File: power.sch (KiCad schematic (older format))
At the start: 8 parts, among them U24 TLV62569P

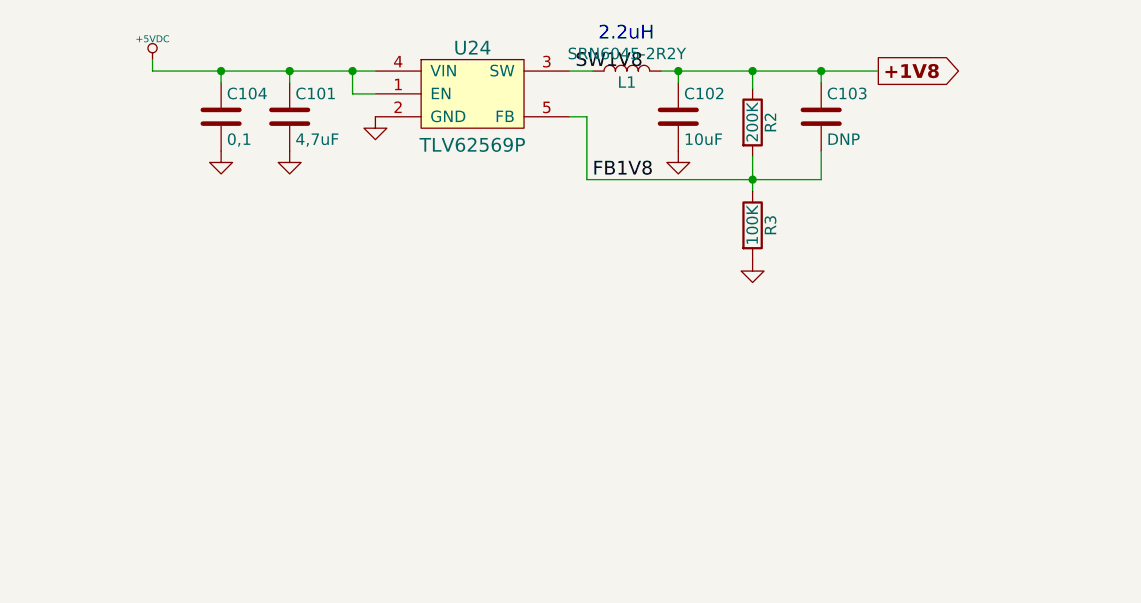
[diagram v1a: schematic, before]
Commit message: +3V3 PSU
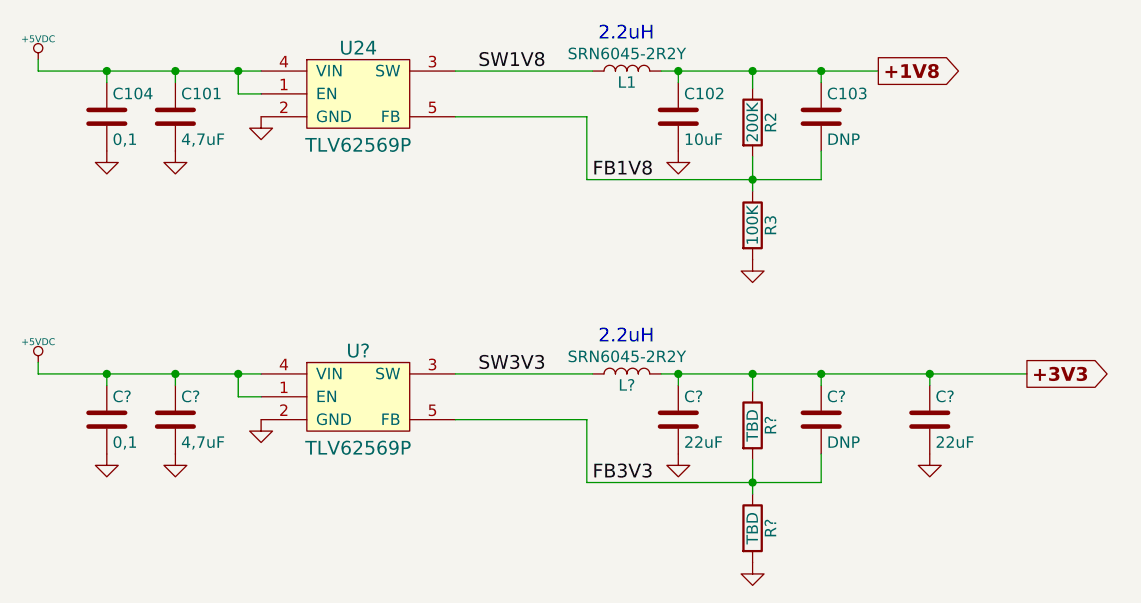
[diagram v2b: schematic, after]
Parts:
- added C?: 4,7uF, Capacitors_SMD:C_0805, symbol C
- added C? (x2): 22uF, Capacitors_Tantalum_SMD:CP_Tantalum_Case-B_EIA-3528-21_Reflow, symbol C
- added C?: DNP, Capacitors_SMD:C_0603, symbol C
- added C?: 0,1, Capacitors_SMD:C_0603, symbol C
- added L?: SRN6045-2R2Y, zorro:SRN6045, symbol L
- added R? (x2): TBD, Resistors_SMD:R_0603, symbol R
- added U?: TLV62569P, TO_SOT_Packages_SMD:SOT-23-5, symbol TLV62569P
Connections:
- net +5VDC: now also C?.1, C?.1, U?.1 (EN), U?.4 (VIN)
- net GND: now also C?.2, C?.2, C?.2, C?.2, R?.2, U?.2 (GND)
- new net +3V3: C?.1, C?.1, C?.1, L?.2, R?.1
- new net FB3V3: C?.2, R?.1, R?.2, U?.5 (FB)
- new net SW3V3: L?.1, U?.3 (SW)
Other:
- moved on the sheet: C101, C104, U24

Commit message: +3V3 placement and early routing
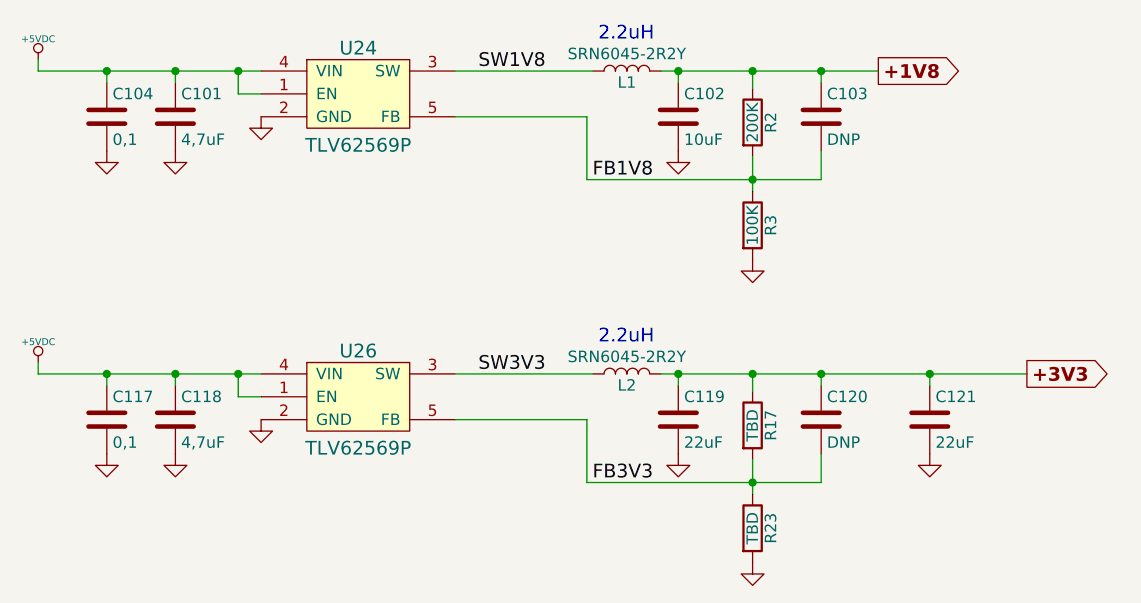
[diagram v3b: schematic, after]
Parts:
- gave numbers to parts that had none: 9
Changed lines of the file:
@@
 $EndComp
 $Comp
-L GND #PWR0178
+L GND #PWR179
 U 1 1 588CA667
 P 4500 3850
-F 0 "#PWR0178" H 4500 3600 50  0001 C CNN
+F 0 "#PWR179" H 4500 3600 50  0001 C CNN
 F 1 "GND" H 4500 3700 50  0001 C CNN
 F 2 "" H 4500 3850 50  0000 C CNN
@@
 	4500 3750 4400 3750
 Wire Wire Line
-	4400 3650 4400 3750
+	4400 3750 4400 3650
 Wire Wire Line
 	3525 3650 4500 3650
@@
 Connection ~ 4125 3650
 $Comp
-L GND #PWR0179
+L GND #PWR181
 U 1 1 588CA72B
 P 4125 4000
-F 0 "#PWR0179" H 4125 3750 50  0001 C CNN
+F 0 "#PWR181" H 4125 3750 50  0001 C CNN
 F 1 "GND" H 4125 3850 50  0001 C CNN
 F 2 "" H 4125 4000 50  0000 C CNN
@@
 	6650 4025 6650 4175
 $Comp
-L GND #PWR0180
+L GND #PWR183
 U 1 1 588CB06D
 P 6650 4475
-F 0 "#PWR0180" H 6650 4225 50  0001 C CNN
+F 0 "#PWR183" H 6650 4225 50  0001 C CNN
 F 1 "GND" H 6650 4325 50  0001 C CNN
 F 2 "" H 6650 4475 50  0000 C CNN
@@
 $EndComp
 $Comp
-L GND #PWR0181
+L GND #PWR182
 U 1 1 588CB1AB
 P 6325 4000
-F 0 "#PWR0181" H 6325 3750 50  0001 C CNN
+F 0 "#PWR182" H 6325 3750 50  0001 C CNN
 F 1 "GND" H 6325 3850 50  0001 C CNN
 F 2 "" H 6325 4000 50  0000 C CNN
@@
 +1V8
 $Comp
-L +5VDC #PWR0182
+L +5VDC #PWR178
 U 1 1 588CF502
 P 3525 3600
-F 0 "#PWR0182" H 3625 3650 20  0001 C CNN
+F 0 "#PWR178" H 3625 3650 20  0001 C CNN
 F 1 "+5VDC" H 3525 3690 30  0000 C CNN
 F 2 "" H 3525 3600 60  0000 C CNN
@@
 Connection ~ 3825 3650
 $Comp
-L GND #PWR0183
+L GND #PWR180
 U 1 1 588D28B5
 P 3825 4000
-F 0 "#PWR0183" H 3825 3750 50  0001 C CNN
+F 0 "#PWR180" H 3825 3750 50  0001 C CNN
 F 1 "GND" H 3825 3850 50  0001 C CNN
 F 2 "" H 3825 4000 50  0000 C CNN
@@
 SW1V8
 $Comp
-L TLV62569P U?
+L TLV62569P U26
 U 1 1 58A65160
 P 4925 5075
-F 0 "U?" H 4925 5275 60  0000 C CNN
+F 0 "U26" H 4925 5275 60  0000 C CNN
 F 1 "TLV62569P" H 4925 4850 60  0000 C CNN
 F 2 "TO_SOT_Packages_SMD:SOT-23-5" H 4925 5075 60  0001 C CNN
@@
 $EndComp
 $Comp
-L GND #PWR?
+L GND #PWR185
 U 1 1 58A65167
 P 4500 5175
-F 0 "#PWR?" H 4500 4925 50  0001 C CNN
+F 0 "#PWR185" H 4500 4925 50  0001 C CNN
 F 1 "GND" H 4500 5025 50  0001 C CNN
 F 2 "" H 4500 5175 50  0000 C CNN
@@
 	4500 5075 4400 5075
 Wire Wire Line
-	4400 4975 4400 5075
+	4400 5075 4400 4975
 Wire Wire Line
 	3525 4975 4500 4975
 Connection ~ 4400 4975
 $Comp
-L C C?
+L C C118
 U 1 1 58A65174
 P 4125 5175
-F 0 "C?" H 4150 5275 50  0000 L CNN
+F 0 "C118" H 4150 5275 50  0000 L CNN
 F 1 "4,7uF" H 4150 5075 50  0000 L CNN
 F 2 "Capacitors_SMD:C_0805" H 4163 5025 50  0001 C CNN
@@
 Connection ~ 4125 4975
 $Comp
-L GND #PWR?
+L GND #PWR187
 U 1 1 58A6517D
 P 4125 5325
-F 0 "#PWR?" H 4125 5075 50  0001 C CNN
+F 0 "#PWR187" H 4125 5075 50  0001 C CNN
 F 1 "GND" H 4125 5175 50  0001 C CNN
 F 2 "" H 4125 5325 50  0000 C CNN
@@
 $EndComp
 $Comp
-L L L?
+L L L2
 U 1 1 58A65183
 P 6100 4975
-F 0 "L?" V 6050 4975 50  0000 C CNN
+F 0 "L2" V 6050 4975 50  0000 C CNN
 F 1 "SRN6045-2R2Y" V 6175 4975 50  0000 C CNN
 F 2 "zorro:SRN6045" H 6100 4975 50  0001 C CNN
@@
 	6250 4975 7850 4975
 $Comp
-L R R?
+L R R17
 U 1 1 58A6518E
 P 6650 5200
-F 0 "R?" V 6730 5200 50  0000 C CNN
+F 0 "R17" V 6730 5200 50  0000 C CNN
 F 1 "TBD" V 6650 5200 50  0000 C CNN
 F 2 "Resistors_SMD:R_0603" V 6580 5200 50  0001 C CNN
@@
 Connection ~ 6650 4975
 $Comp
-L R R?
+L R R23
 U 1 1 58A65196
 P 6650 5650
-F 0 "R?" V 6730 5650 50  0000 C CNN
+F 0 "R23" V 6730 5650 50  0000 C CNN
 F 1 "TBD" V 6650 5650 50  0000 C CNN
 F 2 "Resistors_SMD:R_0603" V 6580 5650 50  0001 C CNN
@@
 	6650 5350 6650 5500
 $Comp
-L GND #PWR?
+L GND #PWR190
 U 1 1 58A6519F
 P 6650 5800
-F 0 "#PWR?" H 6650 5550 50  0001 C CNN
+F 0 "#PWR190" H 6650 5550 50  0001 C CNN
 F 1 "GND" H 6650 5650 50  0001 C CNN
 F 2 "" H 6650 5800 50  0000 C CNN
@@
 Connection ~ 6650 5450
 $Comp
-L C C?
+L C C119
 U 1 1 58A651AA
 P 6325 5175
-F 0 "C?" H 6350 5275 50  0000 L CNN
+F 0 "C119" H 6350 5275 50  0000 L CNN
 F 1 "22uF" H 6350 5075 50  0000 L CNN
 F 2 "Capacitors_Tantalum_SMD:CP_Tantalum_Case-B_EIA-3528-21_Reflow" H 6363 5025 50  0001 C CNN
@@
 $EndComp
 $Comp
-L GND #PWR?
+L GND #PWR188
 U 1 1 58A651B1
 P 6325 5325
-F 0 "#PWR?" H 6325 5075 50  0001 C CNN
+F 0 "#PWR188" H 6325 5075 50  0001 C CNN
 F 1 "GND" H 6325 5175 50  0001 C CNN
 F 2 "" H 6325 5325 50  0000 C CNN
@@
 Connection ~ 6325 4975
 $Comp
-L C C?
+L C C120
 U 1 1 58A651B9
 P 6950 5175
-F 0 "C?" H 6975 5275 50  0000 L CNN
+F 0 "C120" H 6975 5275 50  0000 L CNN
 F 1 "DNP" H 6975 5075 50  0000 L CNN
 F 2 "Capacitors_SMD:C_0603" H 6988 5025 50  0001 C CNN
@@
 +3V3
 $Comp
-L +5VDC #PWR?
+L +5VDC #PWR184
 U 1 1 58A651C3
 P 3525 4925
-F 0 "#PWR?" H 3625 4975 20  0001 C CNN
+F 0 "#PWR184" H 3625 4975 20  0001 C CNN
 F 1 "+5VDC" H 3525 5015 30  0000 C CNN
 F 2 "" H 3525 4925 60  0000 C CNN
@@
 	3525 4925 3525 4975
 $Comp
-L C C?
+L C C117
 U 1 1 58A651CA
 P 3825 5175
-F 0 "C?" H 3850 5275 50  0000 L CNN
+F 0 "C117" H 3850 5275 50  0000 L CNN
 F 1 "0,1" H 3850 5075 50  0000 L CNN
 F 2 "Capacitors_SMD:C_0603" H 3863 5025 50  0001 C CNN
@@
 Connection ~ 3825 4975
 $Comp
-L GND #PWR?
+L GND #PWR186
 U 1 1 58A651D3
 P 3825 5325
-F 0 "#PWR?" H 3825 5075 50  0001 C CNN
+F 0 "#PWR186" H 3825 5075 50  0001 C CNN
 F 1 "GND" H 3825 5175 50  0001 C CNN
 F 2 "" H 3825 5325 50  0000 C CNN
@@
 SW3V3
 $Comp
-L C C?
+L C C121
 U 1 1 58A65DDC
 P 7425 5175
-F 0 "C?" H 7450 5275 50  0000 L CNN
+F 0 "C121" H 7450 5275 50  0000 L CNN
 F 1 "22uF" H 7450 5075 50  0000 L CNN
 F 2 "Capacitors_Tantalum_SMD:CP_Tantalum_Case-B_EIA-3528-21_Reflow" H 7463 5025 50  0001 C CNN
@@
 $EndComp
 $Comp
-L GND #PWR?
+L GND #PWR189
 U 1 1 58A65EC4
 P 7425 5325
-F 0 "#PWR?" H 7425 5075 50  0001 C CNN
+F 0 "#PWR189" H 7425 5075 50  0001 C CNN
 F 1 "GND" H 7425 5175 50  0001 C CNN
 F 2 "" H 7425 5325 50  0000 C CNN

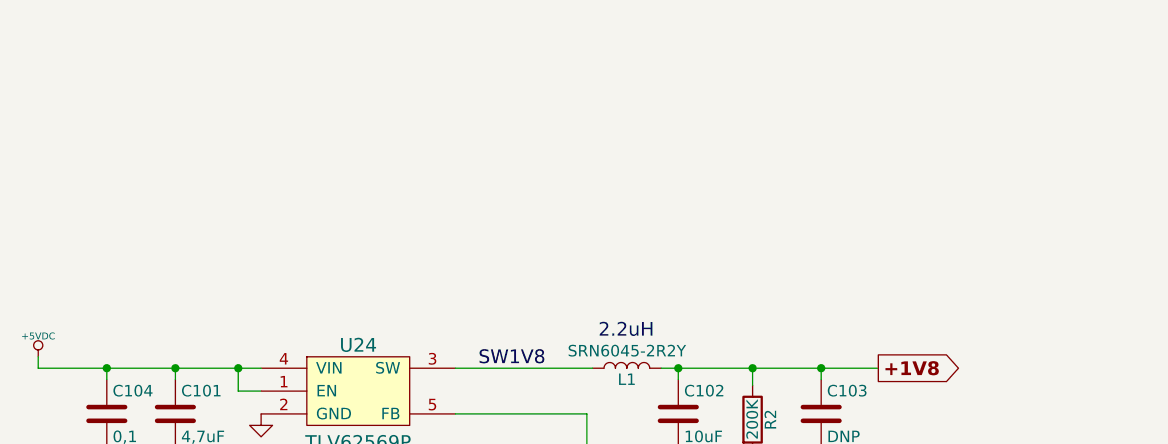
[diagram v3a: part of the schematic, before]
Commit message: Added VCCINT power supply
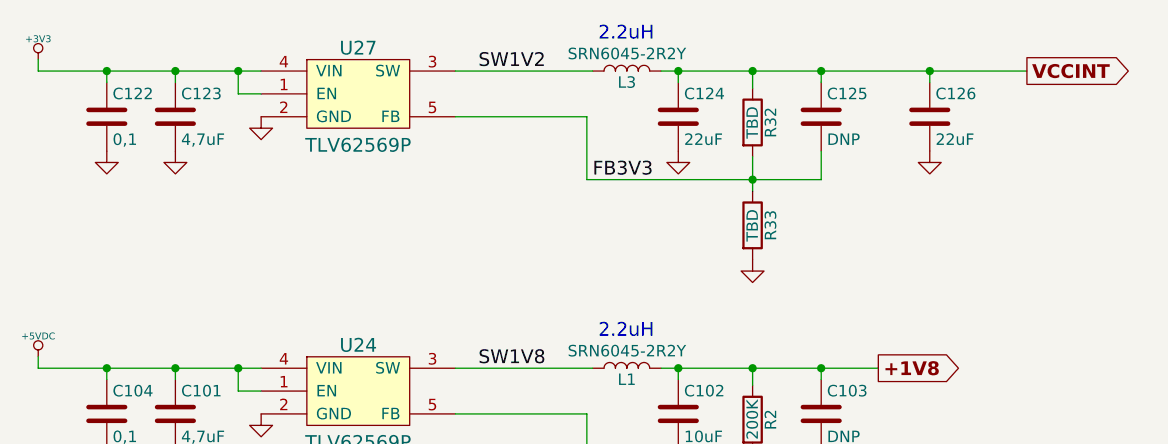
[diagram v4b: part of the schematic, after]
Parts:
- added C122: 0,1, Capacitors_SMD:C_0603, symbol C
- added C123: 4,7uF, Capacitors_SMD:C_0805, symbol C
- added C124, C126: 22uF, Capacitors_Tantalum_SMD:CP_Tantalum_Case-B_EIA-3528-21_Reflow, symbol C
- added C125: DNP, Capacitors_SMD:C_0603, symbol C
- added L3: SRN6045-2R2Y, zorro:SRN6045, symbol L
- added R32, R33: TBD, Resistors_SMD:R_0603, symbol R
- added U27: TLV62569P, TO_SOT_Packages_SMD:SOT-23-5, symbol TLV62569P
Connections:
- net +3V3: now also C122.1, C123.1, U27.1 (EN), U27.4 (VIN)
- net FB3V3: now also C125.2, R32.2, R33.1, U27.5 (FB)
- net GND: now also C122.2, C123.2, C124.2, C126.2, R33.2, U27.2 (GND)
- new net SW1V2: L3.1, U27.3 (SW)
- new net VCCINT: C124.1, C125.1, C126.1, L3.2, R32.1

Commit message: Up
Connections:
- net FB3V3: no longer C125.2, R32.2, R33.1, U27.5 (FB)
- new net FB1V2: C125.2, R32.2, R33.1, U27.5 (FB)
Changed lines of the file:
@@
 $EndComp
 $Comp
-L GND #PWR188
+L GND #PWR0181
 U 1 1 588CA667
 P 4500 3850
-F 0 "#PWR188" H 4500 3600 50  0001 C CNN
+F 0 "#PWR0181" H 4500 3600 50  0001 C CNN
 F 1 "GND" H 4500 3700 50  0001 C CNN
 F 2 "" H 4500 3850 50  0000 C CNN
@@
 Connection ~ 4125 3650
 $Comp
-L GND #PWR185
+L GND #PWR0182
 U 1 1 588CA72B
 P 4125 4000
-F 0 "#PWR185" H 4125 3750 50  0001 C CNN
+F 0 "#PWR0182" H 4125 3750 50  0001 C CNN
 F 1 "GND" H 4125 3850 50  0001 C CNN
 F 2 "" H 4125 4000 50  0000 C CNN
@@
 	6650 4025 6650 4175
 $Comp
-L GND #PWR194
+L GND #PWR0183
 U 1 1 588CB06D
 P 6650 4475
-F 0 "#PWR194" H 6650 4225 50  0001 C CNN
+F 0 "#PWR0183" H 6650 4225 50  0001 C CNN
 F 1 "GND" H 6650 4325 50  0001 C CNN
 F 2 "" H 6650 4475 50  0000 C CNN
@@
 $EndComp
 $Comp
-L GND #PWR191
+L GND #PWR0184
 U 1 1 588CB1AB
 P 6325 4000
-F 0 "#PWR191" H 6325 3750 50  0001 C CNN
+F 0 "#PWR0184" H 6325 3750 50  0001 C CNN
 F 1 "GND" H 6325 3850 50  0001 C CNN
 F 2 "" H 6325 4000 50  0000 C CNN
@@
 +1V8
 $Comp
-L +5VDC #PWR179
+L +5VDC #PWR0185
 U 1 1 588CF502
 P 3525 3600
-F 0 "#PWR179" H 3625 3650 20  0001 C CNN
+F 0 "#PWR0185" H 3625 3650 20  0001 C CNN
 F 1 "+5VDC" H 3525 3690 30  0000 C CNN
 F 2 "" H 3525 3600 60  0000 C CNN
@@
 Connection ~ 3825 3650
 $Comp
-L GND #PWR182
+L GND #PWR0186
 U 1 1 588D28B5
 P 3825 4000
-F 0 "#PWR182" H 3825 3750 50  0001 C CNN
+F 0 "#PWR0186" H 3825 3750 50  0001 C CNN
 F 1 "GND" H 3825 3850 50  0001 C CNN
 F 2 "" H 3825 4000 50  0000 C CNN
@@
 $EndComp
 $Comp
-L GND #PWR189
+L GND #PWR0187
 U 1 1 58A65167
 P 4500 5175
-F 0 "#PWR189" H 4500 4925 50  0001 C CNN
+F 0 "#PWR0187" H 4500 4925 50  0001 C CNN
 F 1 "GND" H 4500 5025 50  0001 C CNN
 F 2 "" H 4500 5175 50  0000 C CNN
@@
 Connection ~ 4125 4975
 $Comp
-L GND #PWR186
+L GND #PWR0188
 U 1 1 58A6517D
 P 4125 5325
-F 0 "#PWR186" H 4125 5075 50  0001 C CNN
+F 0 "#PWR0188" H 4125 5075 50  0001 C CNN
 F 1 "GND" H 4125 5175 50  0001 C CNN
 F 2 "" H 4125 5325 50  0000 C CNN
@@
 	6650 5350 6650 5500
 $Comp
-L GND #PWR195
+L GND #PWR0189
 U 1 1 58A6519F
 P 6650 5800
-F 0 "#PWR195" H 6650 5550 50  0001 C CNN
+F 0 "#PWR0189" H 6650 5550 50  0001 C CNN
 F 1 "GND" H 6650 5650 50  0001 C CNN
 F 2 "" H 6650 5800 50  0000 C CNN
@@
 $EndComp
 $Comp
-L GND #PWR192
+L GND #PWR0190
 U 1 1 58A651B1
 P 6325 5325
-F 0 "#PWR192" H 6325 5075 50  0001 C CNN
+F 0 "#PWR0190" H 6325 5075 50  0001 C CNN
 F 1 "GND" H 6325 5175 50  0001 C CNN
 F 2 "" H 6325 5325 50  0000 C CNN
@@
 Connection ~ 3825 4975
 $Comp
-L GND #PWR183
+L GND #PWR0191
 U 1 1 58A651D3
 P 3825 5325
-F 0 "#PWR183" H 3825 5075 50  0001 C CNN
+F 0 "#PWR0191" H 3825 5075 50  0001 C CNN
 F 1 "GND" H 3825 5175 50  0001 C CNN
 F 2 "" H 3825 5325 50  0000 C CNN
@@
 $EndComp
 $Comp
-L GND #PWR197
+L GND #PWR0192
 U 1 1 58A65EC4
 P 7425 5325
-F 0 "#PWR197" H 7425 5075 50  0001 C CNN
+F 0 "#PWR0192" H 7425 5075 50  0001 C CNN
 F 1 "GND" H 7425 5175 50  0001 C CNN
 F 2 "" H 7425 5325 50  0000 C CNN
@@
 Connection ~ 7425 4975
 $Comp
-L +5VDC #PWR180
+L +5VDC #PWR0193
 U 1 1 58A651C3
 P 3525 4925
-F 0 "#PWR180" H 3625 4975 20  0001 C CNN
+F 0 "#PWR0193" H 3625 4975 20  0001 C CNN
 F 1 "+5VDC" H 3525 5015 30  0000 C CNN
 F 2 "" H 3525 4925 60  0000 C CNN
@@
 $EndComp
 $Comp
-L GND #PWR187
+L GND #PWR0194
 U 1 1 58A865FA
 P 4500 2550
-F 0 "#PWR187" H 4500 2300 50  0001 C CNN
+F 0 "#PWR0194" H 4500 2300 50  0001 C CNN
 F 1 "GND" H 4500 2400 50  0001 C CNN
 F 2 "" H 4500 2550 50  0000 C CNN
@@
 Connection ~ 4125 2350
 $Comp
-L GND #PWR184
+L GND #PWR0195
 U 1 1 58A8660D
 P 4125 2700
-F 0 "#PWR184" H 4125 2450 50  0001 C CNN
+F 0 "#PWR0195" H 4125 2450 50  0001 C CNN
 F 1 "GND" H 4125 2550 50  0001 C CNN
 F 2 "" H 4125 2700 50  0000 C CNN
@@
 	6650 2725 6650 2875
 $Comp
-L GND #PWR193
+L GND #PWR0196
 U 1 1 58A8662B
 P 6650 3175
-F 0 "#PWR193" H 6650 2925 50  0001 C CNN
+F 0 "#PWR0196" H 6650 2925 50  0001 C CNN
 F 1 "GND" H 6650 3025 50  0001 C CNN
 F 2 "" H 6650 3175 50  0000 C CNN
@@
 $EndComp
 $Comp
-L GND #PWR190
+L GND #PWR0197
 U 1 1 58A8663C
 P 6325 2700
-F 0 "#PWR190" H 6325 2450 50  0001 C CNN
+F 0 "#PWR0197" H 6325 2450 50  0001 C CNN
 F 1 "GND" H 6325 2550 50  0001 C CNN
 F 2 "" H 6325 2700 50  0000 C CNN
@@
 Connection ~ 3825 2350
 $Comp
-L GND #PWR181
+L GND #PWR0198
 U 1 1 58A86658
 P 3825 2700
-F 0 "#PWR181" H 3825 2450 50  0001 C CNN
+F 0 "#PWR0198" H 3825 2450 50  0001 C CNN
 F 1 "GND" H 3825 2550 50  0001 C CNN
 F 2 "" H 3825 2700 50  0000 C CNN
@@
 2.2uH
 Text Label 5950 2825 0    60   ~ 0
-FB3V3
+FB1V2
 Text Label 5450 2350 0    60   ~ 0
 SW1V2
@@
 $EndComp
 $Comp
-L GND #PWR196
+L GND #PWR0199
 U 1 1 58A86668
 P 7425 2700
-F 0 "#PWR196" H 7425 2450 50  0001 C CNN
+F 0 "#PWR0199" H 7425 2450 50  0001 C CNN
 F 1 "GND" H 7425 2550 50  0001 C CNN
 F 2 "" H 7425 2700 50  0000 C CNN
@@
 Connection ~ 7425 2350
 $Comp
-L +3V3 #PWR178
+L +3V3 #PWR0200
 U 1 1 58A86765
 P 3525 2300
-F 0 "#PWR178" H 3625 2350 20  0001 C CNN
+F 0 "#PWR0200" H 3625 2350 20  0001 C CNN
 F 1 "+3V3" H 3525 2390 30  0000 C CNN
 F 2 "" H 3525 2300 60  0000 C CNN
